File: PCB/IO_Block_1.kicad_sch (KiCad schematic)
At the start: 12 parts, among them IC1 TLP172AM_TPR,E, IC2 TLP172AM_TPR,E, IC3 TLP172AM_TPR,E, IC4 TLP172AM_TPR,E, IC5 TLP172AM_TPR,E, IC6 TLP172AM_TPR,E

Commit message: Finalized generalized design
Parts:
- removed R2, R3, R4, R5, R6: 150, symbol Device:R
- added R1, R2, R3, R4, R5: RK73B2ETTD151J, RESC3226X70N, symbol RK73B2ETTD151J:RK73B2ETTD151J
- R6: renamed from R1; value 150 -> RK73B2ETTD151J; footprint (none) -> RESC3226X70N; symbol Device:R -> RK73B2ETTD151J:RK73B2ETTD151J; Height (none) -> 0.7; Manufacturer_Name (none) -> KOA Speer; Manufacturer_Part_Number (none) -> RK73B2ETTD151J; Mouser Part Number (none) -> 660-RK73B2ETTD151J; Mouser Price/Stock (none) -> https://www.mouser.com/Search/Refine.aspx?Keyword=660-RK73B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
- renumbered IC6 to IC1, IC5 to IC2, IC4 to IC3, IC3 to IC4, IC2 to IC5, IC1 to IC6
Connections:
- net GND: now also R6.2, R1.2, R2.2, R3.2, R4.2, R5.2; no longer R6.1
- net at IC6.3 (CATHODE): now also R6.1; no longer R6.2
- net at IC2.3 (CATHODE): now also R2.1
- net at IC5.3 (CATHODE): now also R5.1
- net at IC1.3 (CATHODE): now also R1.1
- net at IC4.3 (CATHODE): now also R4.1
- net at IC3.3 (CATHODE): now also R3.1

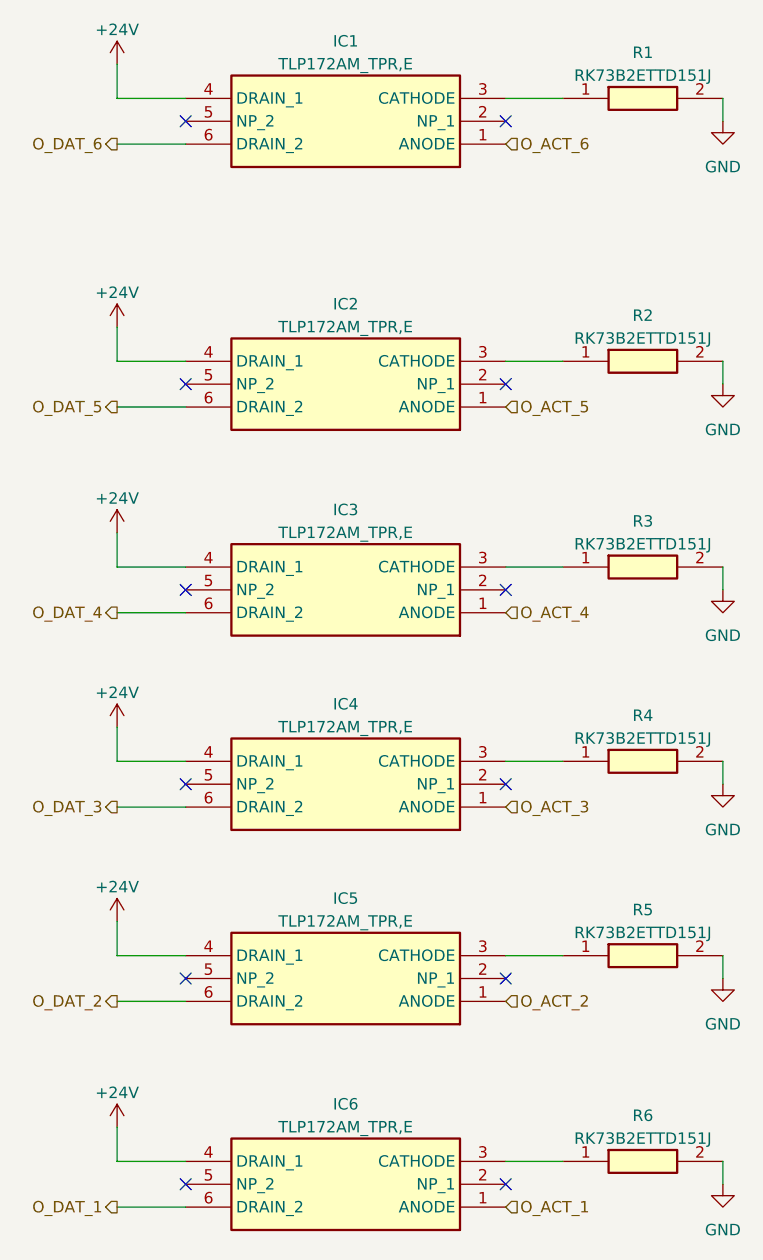
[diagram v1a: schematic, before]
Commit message: Redesigned, to utilize the ESP32 as the basis
* Implemented EEPROM
* Implemented RTC
* Implemented RS232 and 485
* Implemented CANBus
* Implemented everything
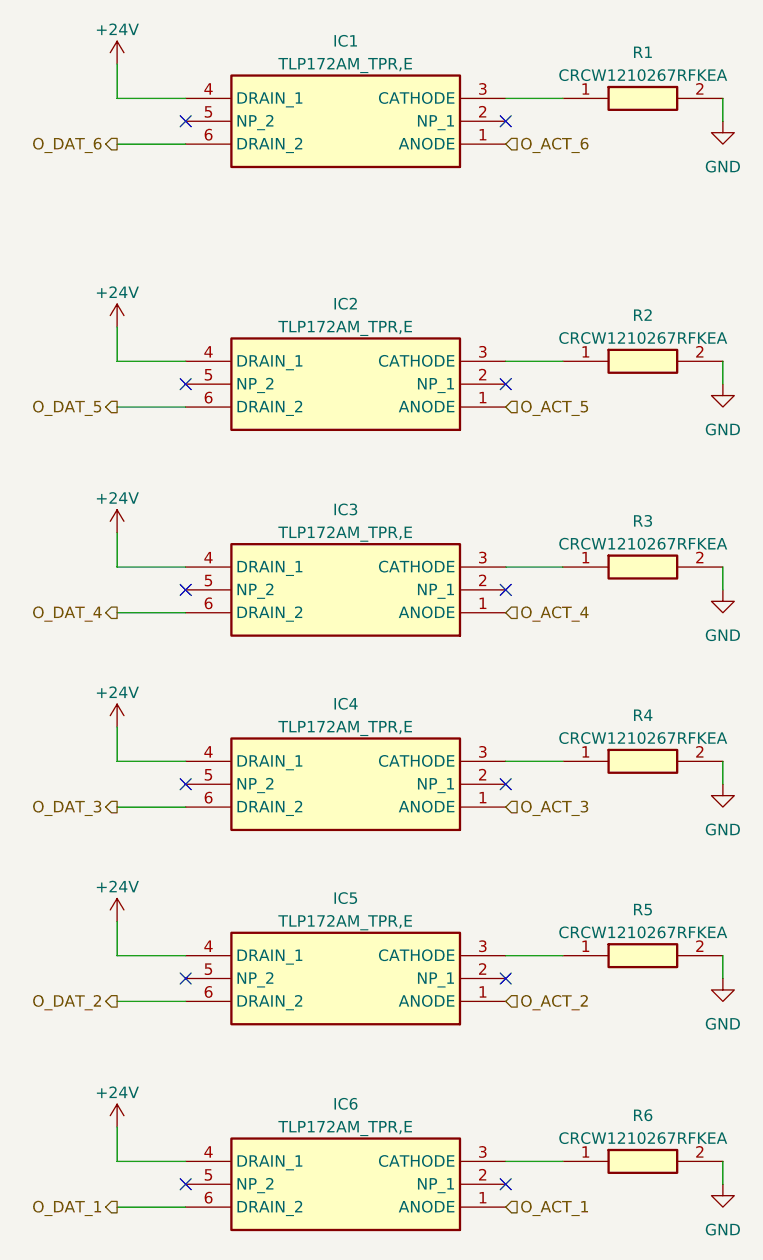
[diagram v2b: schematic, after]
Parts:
- R1, R2, R3, R4, R5, R6: value RK73B2ETTD151J -> CRCW1210267RFKEA; footprint RESC3226X70N -> RESC3225X60N; symbol RK73B2ETTD151J:RK73B2ETTD151J -> CRCW1210267RFKEA:CRCW1210267RFKEA; Height 0.7 -> 0.6; Manufacturer_Name KOA Speer -> Vishay; Manufacturer_Part_Number RK73B2ETTD151J -> CRCW1210267RFKEA; Mouser Part Number 660-RK73B2ETTD151J -> 71-CRCW1210-267-E3; Mouser Price/Stock https://www.mouser.com/Search/Refine.aspx?Keyword=660-RK73B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 -> https://www.mouser.co.uk/ProductDetail/Vishay-Dale/CRCW1210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
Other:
- company: (none) -> UPB - FIIR - Roboți și sisteme de producție
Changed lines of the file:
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@@
 (kicad_sch (version 20230121) (generator eeschema)
   (paper "A4")
+  (title_block
+    (date "2023-04-23")
+    (rev "1")
+    (company "UPB - FIIR - Roboți și sisteme de producție")
+    (comment 1 "Alexandru-Ioan Anastasiu")
+  )

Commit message: Implemented Output block in PCB Started implementation of Input block in PCB
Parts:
- R1, R2, R3, R4, R5, R6: footprint RESC3225X60N -> CRCW1210267RFKEA:RESC3225X60N
